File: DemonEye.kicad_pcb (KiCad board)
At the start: 2 copper layers, 16 x 35.2 mm, 31 parts, among them CN1 PicoBlade 1x06 P1.25mm, Q1 PDTA123EM, Q2 PDTA123EM, Q3 PDTA123EM, Q4 PDTA123EM, Q5 CSD25501F3, U1 WS2814F, U2 TLV76701DRVx, U3 BCR421UFDQ, U4 BCR421UFDQ, U5 BCR421UFDQ, U6 BCR421UFDQ

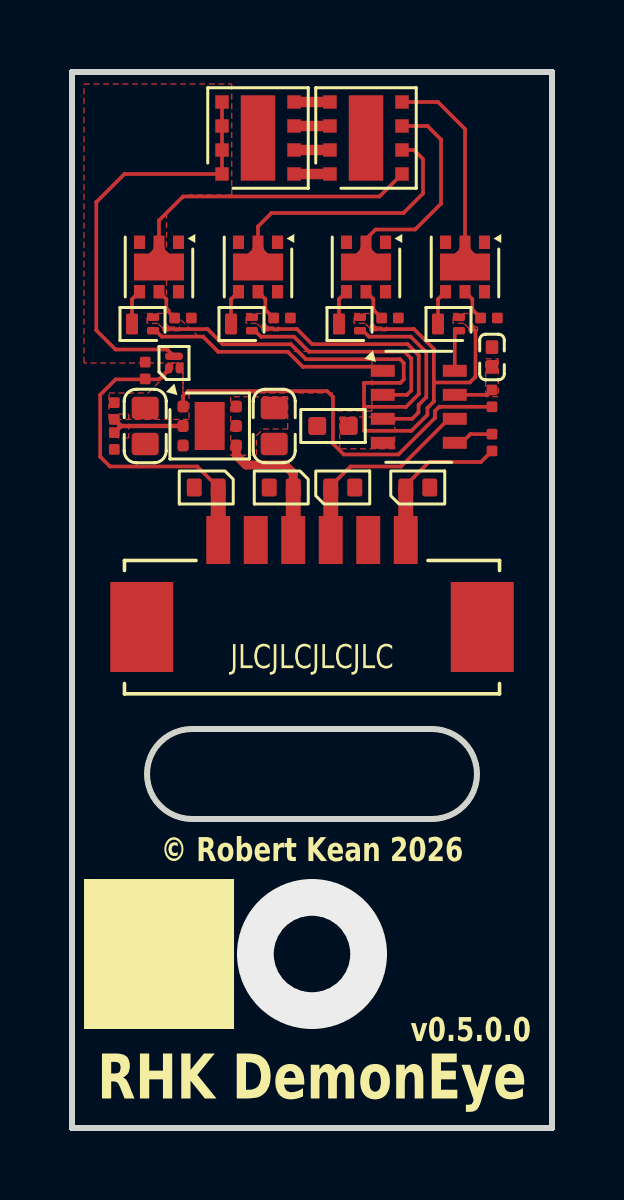
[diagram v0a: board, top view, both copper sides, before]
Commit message: Update .gitignore, DemonEye.kicad_pcb, DemonEye.kicad_prl, and 17 more files
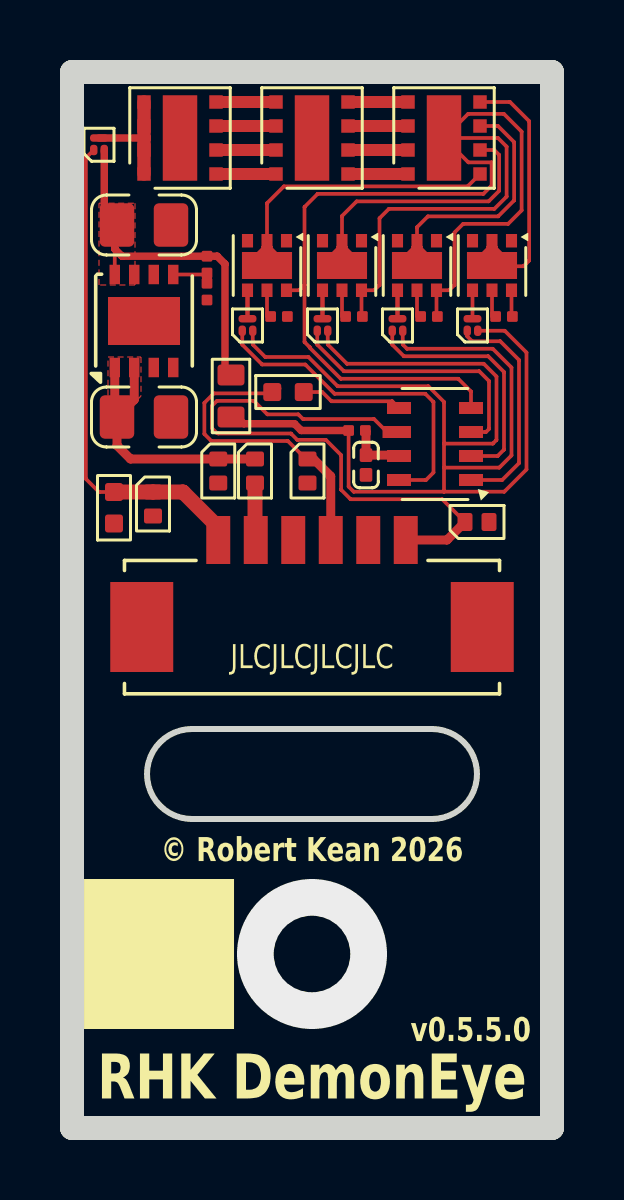
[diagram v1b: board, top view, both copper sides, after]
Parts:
- removed C3: 10uF, My Capacitors:C_0603_Dense
- added C2: 10uF, My Capacitors:C_0805_Nominal, F.Cu at (102.0, 64.5)
- added D5: D_Schottky_Small_Filled, My Package_Leadless:DFN1006-2, F.Cu at (105.7, 72.7)
- added LED3: QLSP06RGBXWAJ, Personal_FootprintLibrary:QLSP06RGBXWAJ, F.Cu at (112.0, 61.6)
- C4: footprint My Capacitors:C_0603_Dense -> My Capacitors:C_0805_Nominal
- Q1, Q2, Q3, Q4: value PDTA123EM -> CSD25501F3; footprint My Package_Leadless:Diodes_DFN1006-3 -> My Package_Leadless:Texas_PICOSTAR-YJN_0.7x0.6mm_PicoStar
- Q5: footprint My Package_Leadless:Texas_-YJN_0.7x0.6mm_PicoStar -> My Package_Leadless:Texas_PICOSTAR-YJN_0.7x0.6mm_PicoStar
- R1: value 1k2 -> 2k7
- R10, R2: footprint My Resistors:R_0201_Dense -> My Resistors:R_0402_Nominal
- R3: footprint My Resistors:R_0402_Nominal -> My Resistors:R_0603_Nominal
- R4, R5, R6, R7: value 20Ω -> 10R5
- R8: value 280k -> 88k7
- R9: value 30k9 -> 10k
- U2: value TLV76701DRVx -> TPL8051Q; footprint My Package_Leadless:WSON-6-1EP_2x2mm_P0.65mm_EP1x1.6mm -> Package_DFN_QFN:DFN-8-1EP_3x3mm_P0.65mm_EP1.55x2.4mm
- moved Q5 7.69 mm to (100.5, 61.8)
- moved R2 7.01 mm to (106.8, 70.1), turned to 0 degrees
- moved R9 5.86 mm to (104.1, 66.7)
- moved R8 5.78 mm to (104.1, 65.8)
- moved C1 5.53 mm to (109.4, 72.5), turned to -90 degrees
- moved R10 4.69 mm to (101.0, 73.9), turned to 90 degrees
- moved R1 4.63 mm to (109.1, 71.3), turned to 180 degrees
- moved D3 4.62 mm to (113.1, 74.4)
- moved C4 4.35 mm to (102.0, 70.9), turned to 0 degrees
- moved U2 4.13 mm to (102.0, 67.7), turned to 90 degrees
- moved D4 3.72 mm to (107.5, 72.7), turned to -90 degrees
- moved U3 3.60 mm to (106.1, 65.8)
- moved R3 3.54 mm to (104.9, 70.2), turned to -90 degrees
- moved Q1 3.50 mm to (105.5, 67.8), turned to 90 degrees
- moved R4 3.20 mm to (106.5, 67.5), turned to 0 degrees
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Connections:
- C4 pad 1: +V_{BAT} -> +V_{IN}
- CN1 pad 2: GND -> /+V_{BAT}
- CN1 pad 3: +V_{BAT} -> GND
- CN1 pad 4: /D_{IN} -> /D_{OUT}
- CN1 pad 6: /D_{OUT} -> /D_{IN}
- D1 pad 1: +V_{BAT} -> +V_{IN}
- LED1 pad 1: +8V_{SW} -> /+12V_{SW}
- LED1 pad 2: +8V_{SW} -> /+12V_{SW}
- LED1 pad 3: +8V_{SW} -> /+12V_{SW}
- LED1 pad 4: +8V_{SW} -> /+12V_{SW}
- Q1 pad 2: +8V_{SW} -> +12V
- Q2 pad 2: +8V_{SW} -> +12V
- Q3 pad 2: +8V_{SW} -> +12V
- Q4 pad 2: +8V_{SW} -> +12V
- Q5 pad 2: +8V -> +V_{OUT}
- Q5 pad 3: +8V_{SW} -> /+12V_{SW}
- R1 pad 2: +8V -> +12V
- R3 pad 1: /GND0 -> +V_{OUT}
- R3 pad 2: GND -> +12V
- R4 pad 1: GND -> /R_{EXT_R}
- R4 pad 2: /R_{EXT_R} -> GND
- R5 pad 1: GND -> /R_{EXT_G}
- R5 pad 2: /R_{EXT_G} -> GND
- R6 pad 1: GND -> /R_{EXT_B}
- R6 pad 2: /R_{EXT_B} -> GND
- R7 pad 1: GND -> /R_{EXT_W}
- R7 pad 2: /R_{EXT_W} -> GND
- R8 pad 1: /FB -> Net-(U2-FB)
- R8 pad 2: +8V -> +V_{OUT}
- R9 pad 2: /FB -> Net-(U2-FB)
- U1 pad 1: /OUTR -> /OUTW
- U1 pad 2: /OUTG -> /OUTB
- U1 pad 3: /OUTB -> /OUTG
- U1 pad 4: /GND0 -> GND
- U1 pad 8: /OUTW -> /OUTR
- U2 pad 1: +8V -> +V_{IN}
- U2 pad 2: /FB -> +V_{IN}
- U2 pad 3: GND -> unconnected-(U2-NC-Pad3)
- U2 pad 4: +V_{BAT} -> GND
- U2 pad 5: GND -> Net-(U2-FB)
- U2 pad 6: +V_{BAT} -> unconnected-(U2-NC-Pad6)
- U2 pad 7: GND -> unconnected-(U2-NC-Pad7)
- U3 pad 2: /Red2 -> /Red
- U4 pad 2: /Green2 -> /Green
- U5 pad 2: /Blue2 -> /Blue
- U6 pad 2: /White2 -> /White
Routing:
- net +12V: track 0.00 -> 48.8 mm
- net GND: track 0.00 -> 46.0 mm
- net +8V_{SW}: track 45.3 -> 0.00 mm
- net /D_{IN}: track 6.86 -> 20.2 mm
- net +8V: track 13.3 -> 0.00 mm
- net +V_{OUT}: track 0.00 -> 12.8 mm
- net +V_{IN}: track 0.00 -> 9.31 mm
- net /Red: track 0.00 -> 8.75 mm
- net /White: track 0.00 -> 8.63 mm
- net /Green: track 0.00 -> 8.31 mm
- net /Red2: track 9.47 -> 2.00 mm
- net /Blue: track 0.00 -> 7.36 mm
- net /Green2: track 8.45 -> 2.00 mm
- net /OUTW: track 1.44 -> 7.51 mm
- net /SRH: track 10.8 -> 16.6 mm
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- added copper zone on F.Cu, net +V_{IN}
- added copper zone on F.Cu, net +V_{OUT}
- removed copper zone on F.Cu, net +8V
- removed copper zone on F.Cu, net +8V_{SW}
- removed copper zone on F.Cu, net +V_{BAT}
- removed copper zone on F.Cu, net /FB
- removed copper zone on F.Cu, net /GND0
- removed copper zone on F.Cu, net /V_{DD}
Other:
- board text added: "v0.5.5.0"
- board text removed: "v0.5.0.0"

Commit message: reworked the protection circuitry for the SRH signal to protect the PFET from surges and >16V load dumps
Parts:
- added D6: 16V, My Package_Leadless:DFN1006-2, F.Cu at (100.6, 74.9)
- added R11: 200R, My Resistors:R_0402_Nominal, F.Cu at (101.9, 73.9)
- R10: value 1k2 -> 10k; footprint My Resistors:R_0402_Nominal -> My Resistors:R_0201_Nominal
- R4, R5, R6, R7: value 10R5 -> 10R
- moved R10 0.97 mm to (100.7, 73.0), turned to -90 degrees
- moved D2 0.90 mm to (103.2, 73.8), turned to 90 degrees
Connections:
- Q5 pad 1: /SRH -> /SRH_{G}
- R10 pad 2: /SRH -> /SRH_{G}
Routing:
- net /SRH_{G}: track 0.00 -> 14.1 mm
- net /SRH: track 16.6 -> 3.26 mm
- added copper zone on F.Cu, net /+12V_{SW}
- added copper zone on F.Cu, net /Blue
- added copper zone on F.Cu, net /Green
- added copper zone on F.Cu, net /Red
- added copper zone on F.Cu, net /White
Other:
- board text added: "v0.5.5.5"
- board text removed: "v0.5.5.0"

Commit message: V5.5.5, DFM completed
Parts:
- moved R6 0.30 mm to (111.8, 67.5)
- moved R4 0.20 mm to (106.7, 67.5)
- moved R5 0.20 mm to (109.2, 67.5)
- moved R7 0.20 mm to (114.2, 67.5)
- moved C1 0.10 mm to (109.4, 72.6)
